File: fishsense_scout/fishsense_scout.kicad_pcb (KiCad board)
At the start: 2 copper layers, 1 part, among them U1 LMR16030PDDA

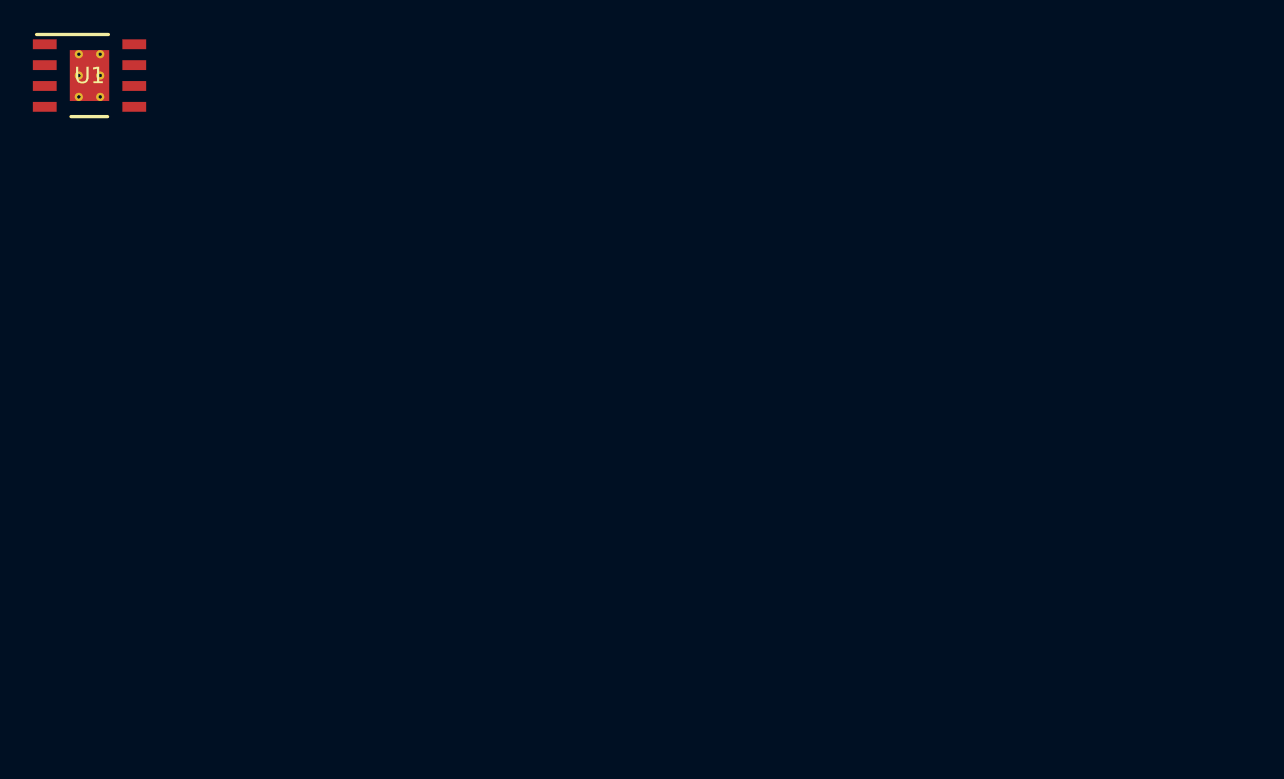
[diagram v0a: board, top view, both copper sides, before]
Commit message: Finished PCB schematic design along with ERC check, assigned footprints, and made rough arrangement of components in PCB
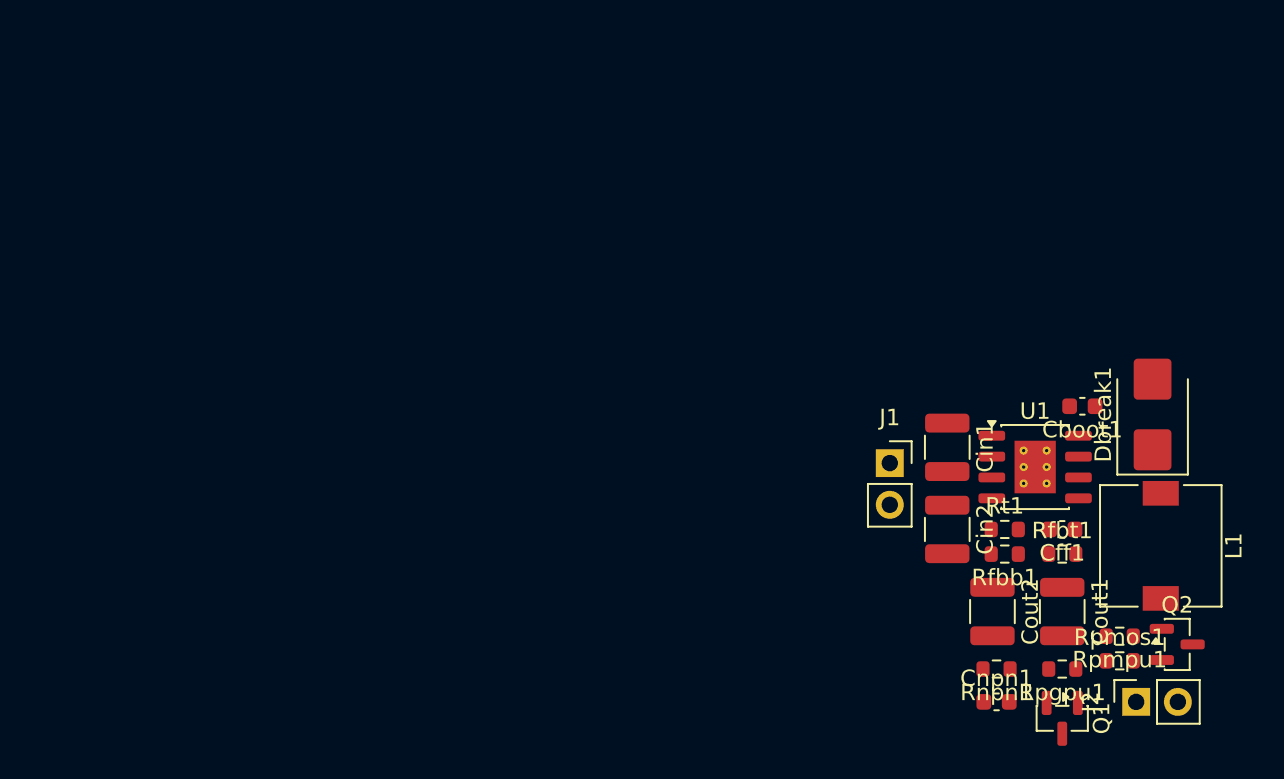
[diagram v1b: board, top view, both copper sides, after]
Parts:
- added Cboot1: 100nF, Capacitor_SMD:C_0603_1608Metric, F.Cu at (154.7, 79.0)
- added Cff1: 390pF, Capacitor_SMD:C_0603_1608Metric, F.Cu at (153.5, 86.5)
- added Cin1: 2.2uF, Capacitor_SMD:C_1210_3225Metric, F.Cu at (146.5, 81.5)
- added Cin2: 2.2uF, Capacitor_SMD:C_1210_3225Metric, F.Cu at (146.5, 86.5)
- added Cnpn1: 47nF, Capacitor_SMD:C_0603_1608Metric, F.Cu at (149.5, 97.0)
- added Cout1: 47uF, Capacitor_SMD:C_1210_3225Metric, F.Cu at (153.5, 91.5)
- added Cout2: 47uF, Capacitor_SMD:C_1210_3225Metric, F.Cu at (149.2, 91.5)
- added Dbreak1: D_Schottky, Diode_SMD:D_SMB, F.Cu at (159.0, 79.5)
- added J1: Conn_01x02_Pin, Connector_PinSocket_2.54mm:PinSocket_1x02_P2.54mm_Vertical, F.Cu at (143.0, 82.5)
- added J2: Conn_01x02_Pin, Connector_PinSocket_2.54mm:PinSocket_1x02_P2.54mm_Vertical, F.Cu at (158.0, 97.0)
- added L1: 8.2uH, Inductor_SMD:L_7.3x7.3_H3.5, F.Cu at (159.5, 87.5)
- added Q1: NPN, Package_TO_SOT_SMD:SOT-23, F.Cu at (153.5, 98.0)
- added Q2: PMOS, Package_TO_SOT_SMD:SOT-23, F.Cu at (160.5, 93.5)
- added Rfbb1: 12k, Resistor_SMD:R_0603_1608Metric, F.Cu at (150.0, 88.0)
- added Rfbt1: 68k, Resistor_SMD:R_0603_1608Metric, F.Cu at (153.5, 88.0)
- added Rnpn1: 10k, Resistor_SMD:R_0603_1608Metric, F.Cu at (149.5, 95.0)
- added Rpgpu1: 47k, Resistor_SMD:R_0603_1608Metric, F.Cu at (153.5, 95.0)
- added Rpmos1: 100, Resistor_SMD:R_0603_1608Metric, F.Cu at (157.0, 94.5)
- added Rpmpu1: 100k, Resistor_SMD:R_0603_1608Metric, F.Cu at (157.0, 93.0)
- added Rt1: 45.3k, Resistor_SMD:R_0603_1608Metric, F.Cu at (150.0, 86.5)
- U1: footprint LMR16030:DDA0008E_N -> Package_SO:SOIC-8-1EP_3.9x4.9mm_P1.27mm_EP2.514x3.2mm_ThermalVias
- moved U1 62.3 mm to (151.8, 82.7)
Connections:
- U1 pad 1: unconnected-(U1-BOOT-Pad1) -> Net-(U1-BOOT)
- U1 pad 2: unconnected-(U1-VIN-Pad2) -> /Vin
- U1 pad 3: unconnected-(U1-EN-Pad3) -> /Vin
- U1 pad 4: unconnected-(U1-RT_SYNC-Pad4) -> Net-(U1-RT_SYNC)
- U1 pad 5: unconnected-(U1-FB-Pad5) -> Net-(U1-FB)
- U1 pad 6: unconnected-(U1-PWRGD-Pad6) -> Net-(U1-PWRGD)
- U1 pad 7: unconnected-(U1-GND-Pad7) -> GNDPWR
- U1 pad 8: unconnected-(U1-SW-Pad8) -> Net-(Dbreak1-K)
- U1 pad 9: unconnected-(U1-PAD-Pad9) -> GNDPWR

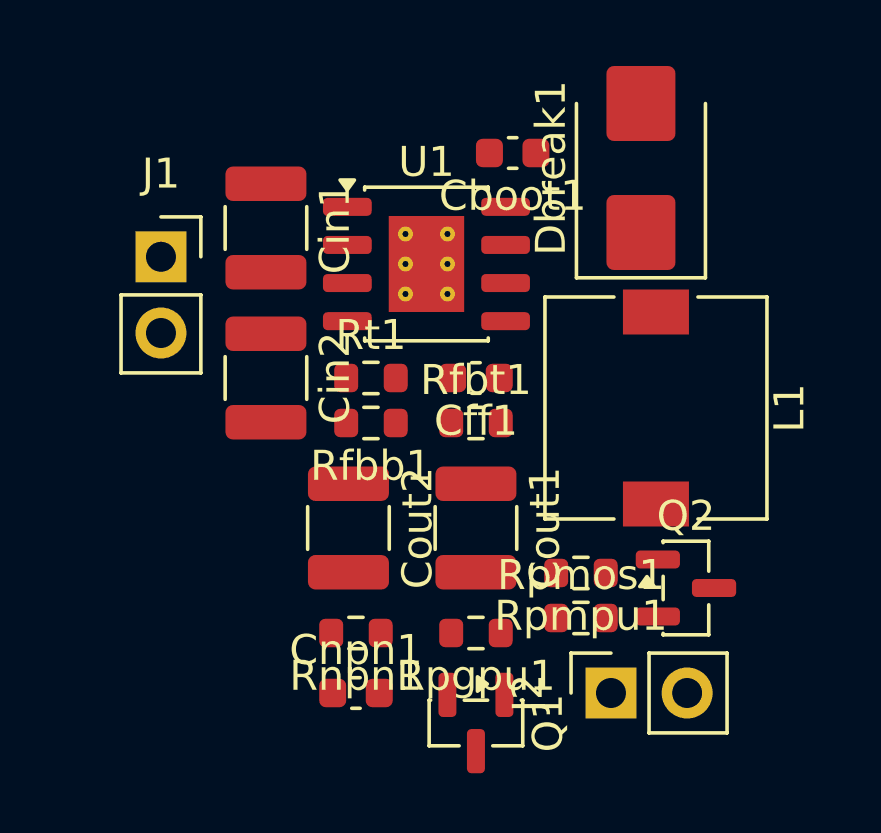
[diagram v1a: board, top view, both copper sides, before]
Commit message: Small arrangementtweaks
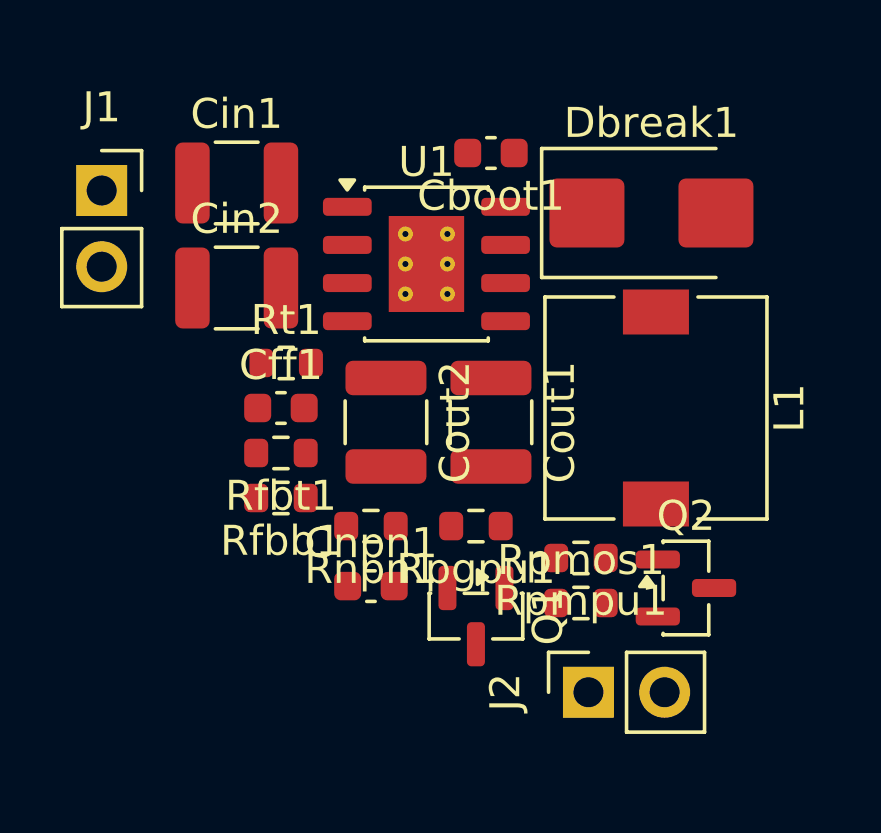
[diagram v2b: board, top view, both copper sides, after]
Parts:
- moved Cff1 6.58 mm to (147.0, 87.5), turned to 0 degrees
- moved Rfbt1 6.58 mm to (147.0, 89.0), turned to 180 degrees
- moved Rfbb1 3.91 mm to (147.0, 90.5)
- moved Cout2 3.74 mm to (150.5, 88.0)
- moved Cnpn1 3.60 mm to (150.0, 93.4)
- moved Rnpn1 3.60 mm to (150.0, 91.4)
- moved Q1 3.56 mm to (153.5, 94.4)
- moved Rpgpu1 3.56 mm to (153.5, 91.4)
- moved Cout1 3.56 mm to (154.0, 88.0)
- moved Cin2 3.15 mm to (145.5, 83.5), turned to 0 degrees
- moved J1 2.96 mm to (141.0, 80.2)
- moved Rt1 2.87 mm to (147.2, 86.0)
- moved Cin1 1.79 mm to (145.5, 80.0), turned to 0 degrees
- moved Dbreak1 1.54 mm to (159.3, 81.0), turned to 0 degrees
- moved J2 0.75 mm to (157.2, 97.0)
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
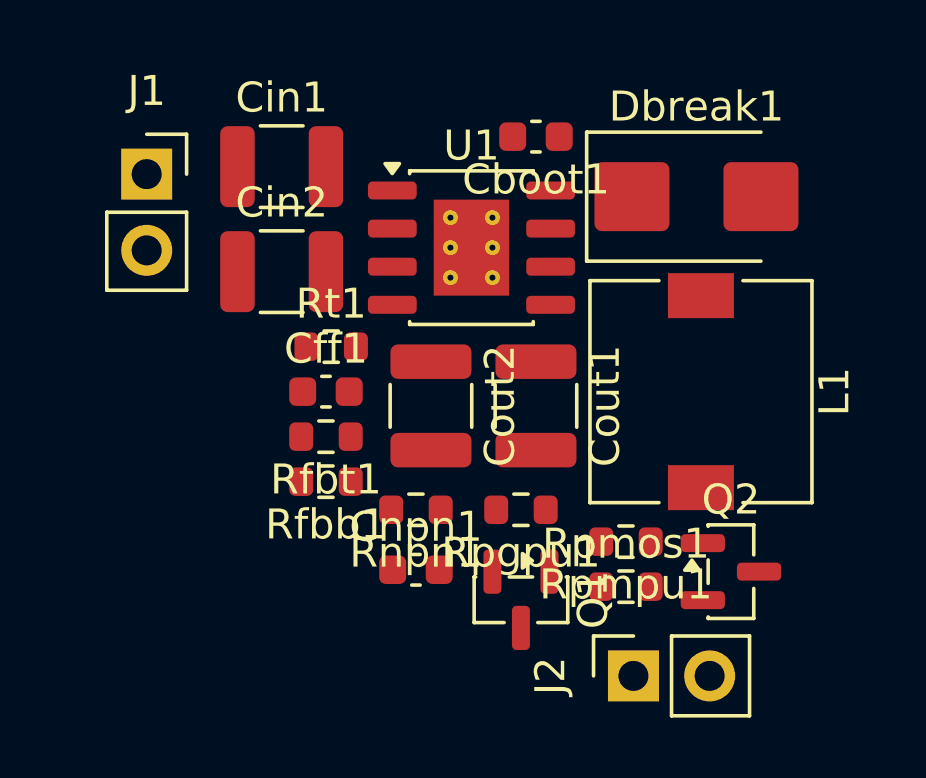
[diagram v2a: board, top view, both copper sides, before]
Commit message: Added traces and rearranged footprints slightly to accomodate for traces
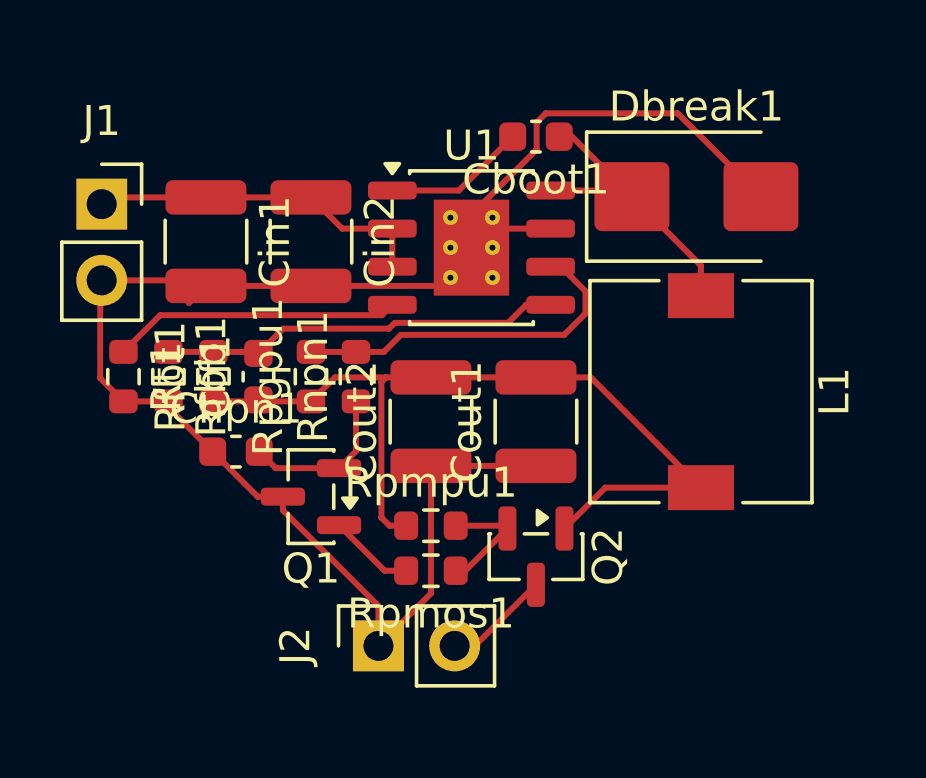
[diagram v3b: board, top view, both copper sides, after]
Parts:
- moved J2 8.56 mm to (148.8, 96.0)
- moved Rpgpu1 8.29 mm to (146.5, 87.0), turned to 90 degrees
- moved Q1 7.80 mm to (146.5, 91.0), turned to 180 degrees
- moved Cnpn1 7.18 mm to (144.0, 89.5)
- moved Rt1 7.00 mm to (140.2, 87.0), turned to -90 degrees
- moved Rpmos1 6.52 mm to (150.5, 93.5), turned to 180 degrees
- moved Rpmpu1 6.52 mm to (150.5, 92.0), turned to 0 degrees
- moved Q2 6.52 mm to (154.0, 93.0), turned to -90 degrees
- moved Rfbb1 6.31 mm to (141.8, 87.0), turned to -90 degrees
- moved Rnpn1 4.87 mm to (148.0, 87.0), turned to 90 degrees
- moved Rfbt1 4.25 mm to (143.2, 87.0), turned to 90 degrees
- moved Cin1 3.55 mm to (143.0, 82.5), turned to -90 degrees
- moved Cff1 2.30 mm to (144.8, 87.0), turned to 90 degrees
- moved J1 1.80 mm to (139.5, 81.2)
- moved Cin2 1.40 mm to (146.5, 82.5), turned to -90 degrees
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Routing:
- net GNDPWR: track 0.00 -> 56.6 mm
- net Net-(Q2-D): track 0.00 -> 29.7 mm
- net Net-(U1-FB): track 0.00 -> 13.6 mm
- net Net-(U1-PWRGD): track 0.00 -> 11.9 mm
- net /Vin: track 0.00 -> 11.5 mm
- net Net-(Dbreak1-K): track 0.00 -> 10.3 mm
- net Net-(U1-RT_SYNC): track 0.00 -> 10.0 mm
- net Net-(Q1-B): track 0.00 -> 5.56 mm
- net Net-(U1-BOOT): track 0.00 -> 4.76 mm
- net Net-(Q2-G): track 0.00 -> 4.07 mm
- net /Vout: track 0.00 -> 3.86 mm
- net Net-(Q1-C): track 0.00 -> 2.87 mm

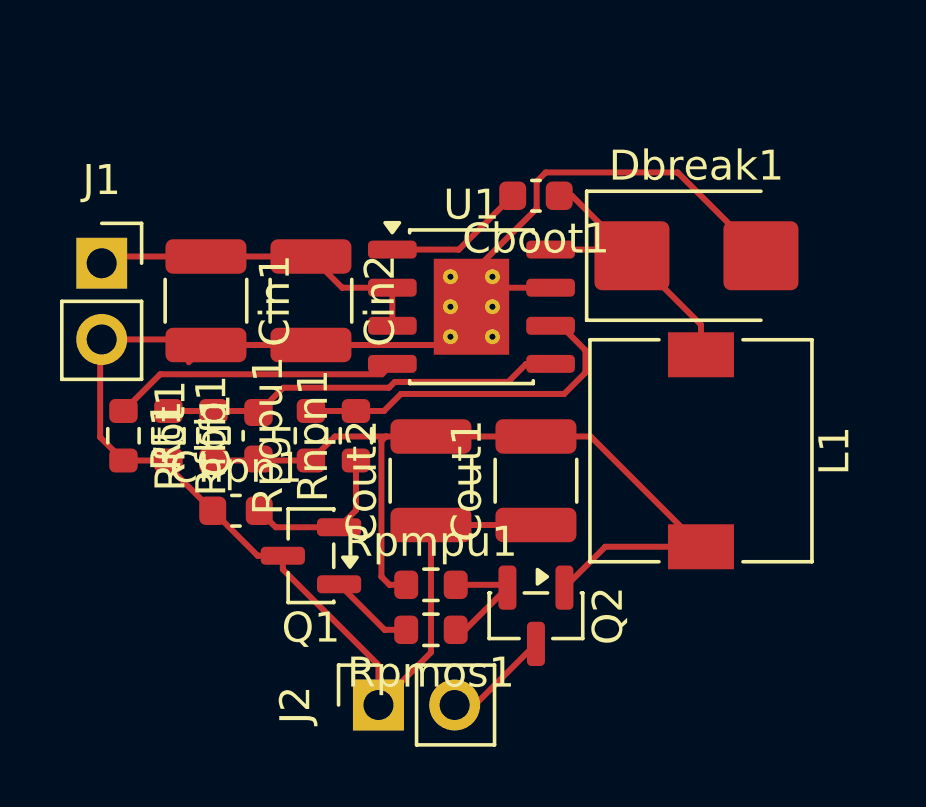
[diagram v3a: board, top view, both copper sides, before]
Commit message: Rearranged traces and added new pin connectors
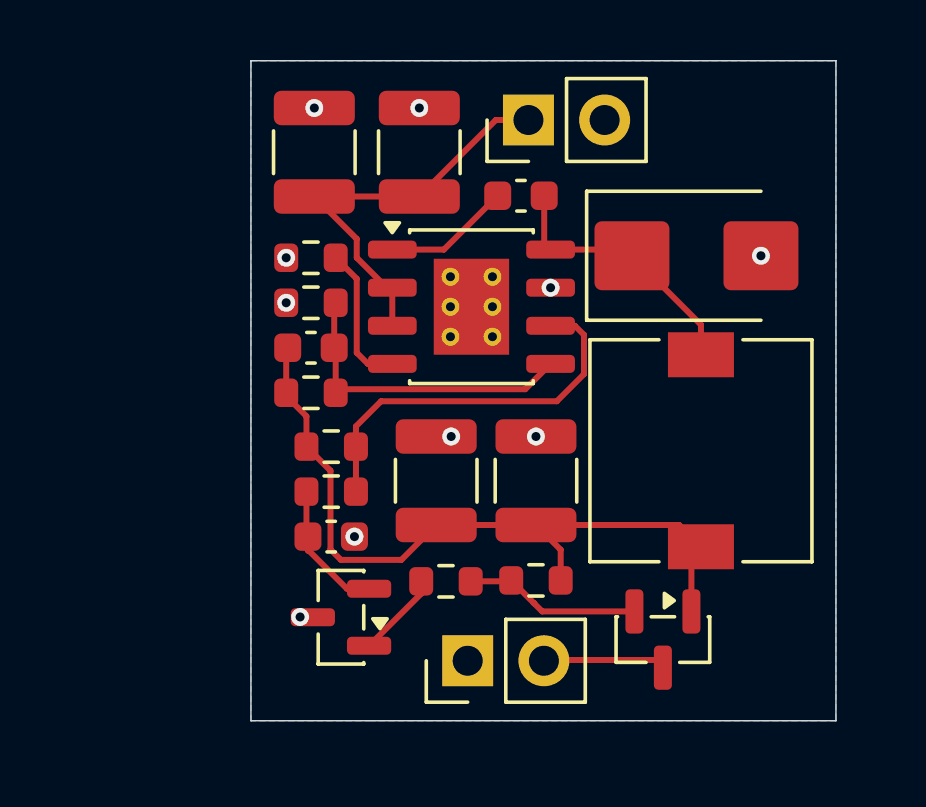
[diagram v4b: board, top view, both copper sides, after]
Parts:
- J1, J2: footprint Connector_PinSocket_2.54mm:PinSocket_1x02_P2.54mm_Vertical -> Connector_PinHeader_2.54mm:PinHeader_1x02_P2.54mm_Vertical
- moved J1 15.0 mm to (153.8, 76.5), turned to 90 degrees
- moved Rt1 8.62 mm to (146.5, 81.1), turned to 180 degrees
- moved Rfbb1 6.50 mm to (146.5, 82.6), turned to 180 degrees
- moved Cin1 6.13 mm to (146.6, 77.5), turned to 90 degrees
- moved Cin2 6.13 mm to (150.1, 77.5), turned to 90 degrees
- moved Q2 4.31 mm to (158.2, 93.8)
- moved Rfbt1 3.55 mm to (146.5, 85.6), turned to 0 degrees
- moved Rpmpu1 3.50 mm to (154.0, 91.8), turned to 180 degrees
- moved Cff1 3.42 mm to (146.5, 84.1), turned to 0 degrees
- moved J2 3.32 mm to (151.7, 94.5)
- moved Cnpn1 3.29 mm to (147.2, 90.4), turned to 180 degrees
- moved Q1 2.28 mm to (147.5, 93.0)
- moved Rnpn1 2.04 mm to (147.2, 88.9), turned to 0 degrees
- moved Rpmos1 1.69 mm to (151.0, 91.9)
- moved Rpgpu1 0.77 mm to (147.2, 87.4), turned to 0 degrees
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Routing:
- net GNDPWR: track 56.6 -> 3.40 mm, vias 0 -> 10
- net Net-(U1-RT_SYNC): track 10.0 -> 4.80 mm
- net Net-(Q2-D): track 29.7 -> 25.6 mm
- net /Vin: track 11.5 -> 14.3 mm
- net Net-(U1-FB): track 13.6 -> 11.2 mm
- net Net-(Q2-G): track 4.07 -> 5.93 mm
- net Net-(Dbreak1-K): track 10.3 -> 8.95 mm
- net Net-(U1-PWRGD): track 11.9 -> 13.0 mm
- net /Vout: track 3.86 -> 3.25 mm
- added copper zone on B.Cu, net GNDPWR
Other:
- board outline added: 19.5 x 22 mm
